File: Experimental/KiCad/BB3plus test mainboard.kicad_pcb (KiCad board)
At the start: 4 copper layers, 180.5 x 176 mm, 290 parts, among them IC1 SN74HCS02PWR, IC10 TPS62933ODRLR, IC11 FUSB303BTMX, IC12 TPS2068E, IC13 RT9742SNGV, IC14 TPD4E001DRLR, IC15 TPD4E001DRLR, IC16 TPD12S016PWR, IC17 MIC2026A-1YM-TR, IC18 TPD4E001DRLR, IC2 TPS3851H18EDRBR, IC3 M24C32-DFDW6TP, IC4 STM32G071R8T6, IC5 TPA6205A1DGN, IC6 SN74LVC1G14DBVR, IC7 LM64460CPPQRYFRQ1, IC8 TPS62933ODRLR, IC9 USB5816C-I/KD, Q1 2N7002, Q2 2N7002, Q3 MMBT5401, Q4 MMBT5401, Q5 2N7002, Q6 DMP3013SFV-7, Q7 DMP3013SFV-7, SW1 WBL2UOAGQR05CLR, SW2 LP4EE1RBATY, SW3 PEC16-2215F-S0024, X1 1-2199230-6, X10 10018783-10101TLF, X11 77313-802-20LF, X12 77313-802-20LF, X13 10018783-10101TLF, X14 5051102091, X15 TBP03R1-350-10BE, X3 571-0400, X4 GSP1.9101.1, X5 PJ-002BH-SMT-TR, X6 USB4056-03-A, X7 0862-1J1T-43-F, X8 SS-53000-002, X9 5051102091, Y1 32.768KHz, Y2 VXM7-9032-25M0000000

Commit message: Gerbers update
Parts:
- X10: value 10018783-10101TLF -> 1001878410201TLF
- moved JP11 0.80 mm to (313.8, 88.2)
- moved JP15 0.80 mm to (412.4, 26.2)
- moved JP3 0.77 mm to (388.3, 109.2)
- moved JP7 0.77 mm to (388.3, 106.7)

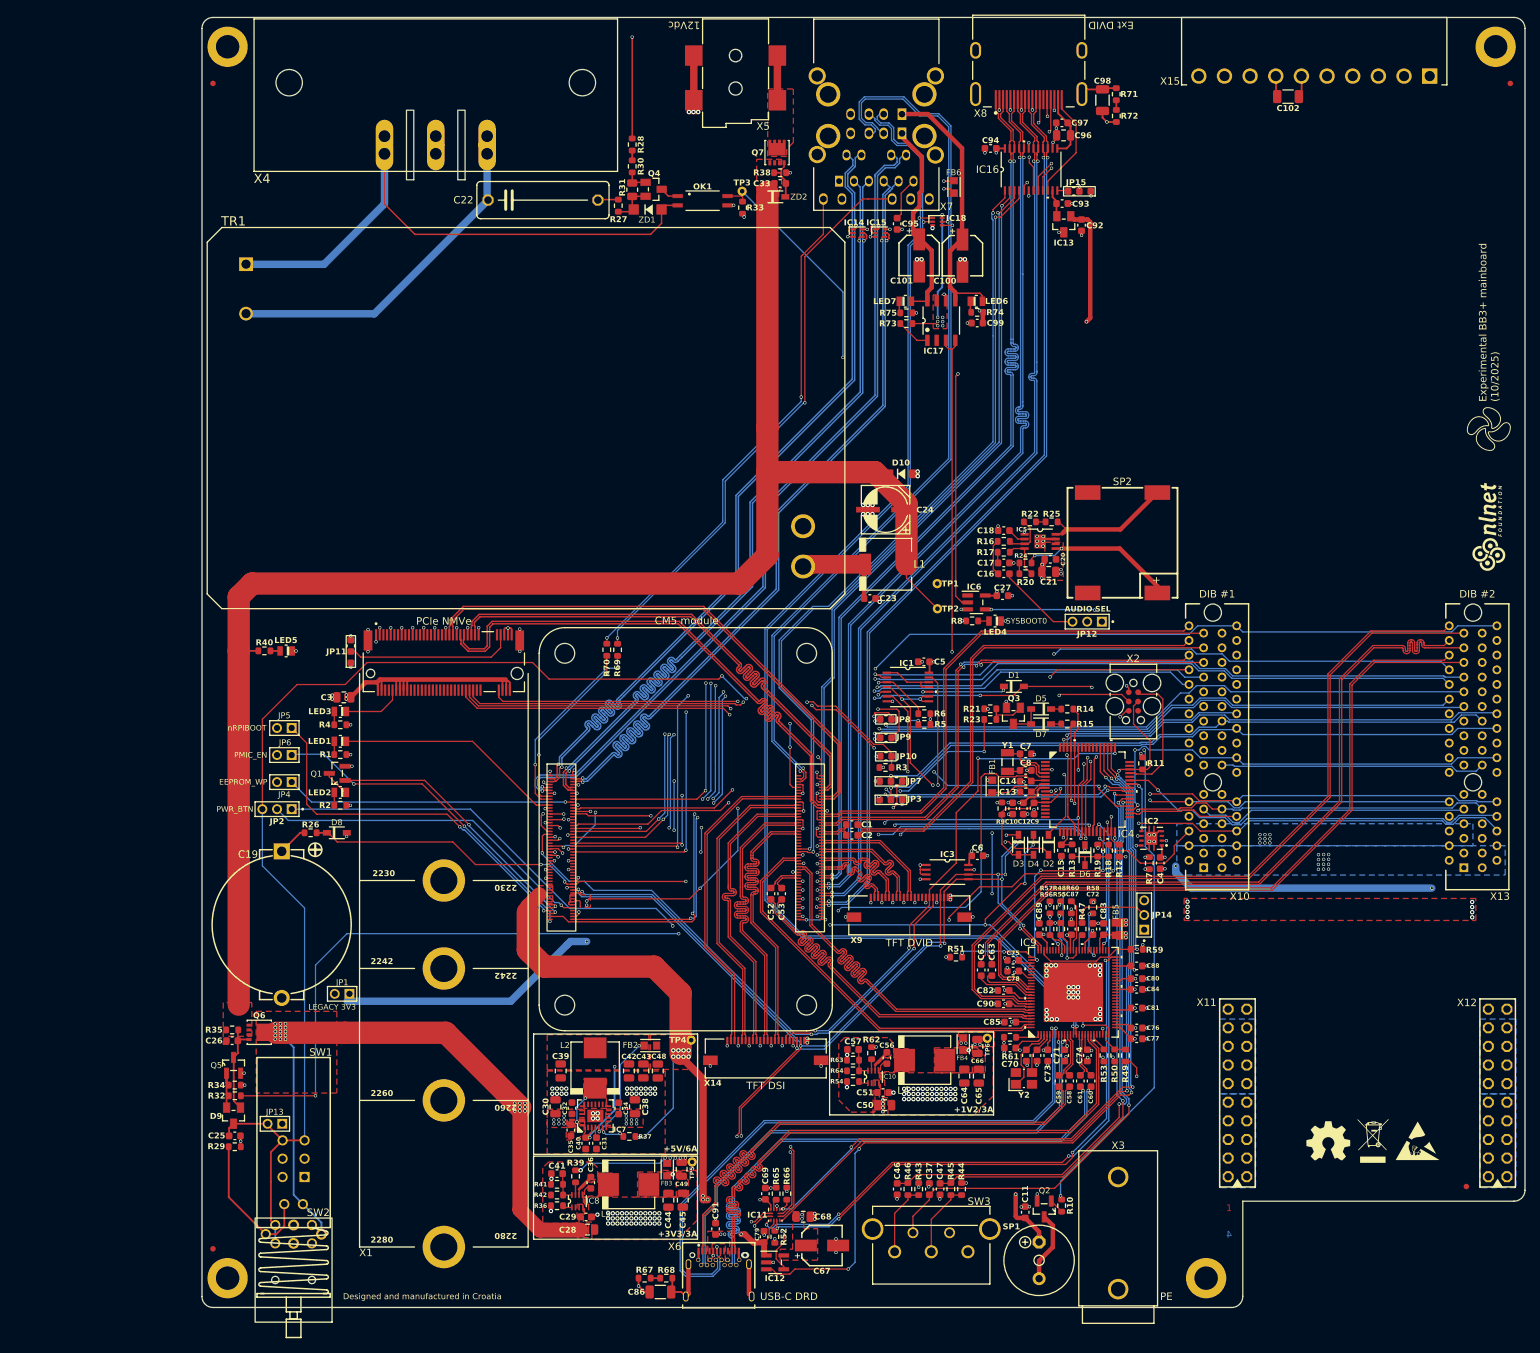
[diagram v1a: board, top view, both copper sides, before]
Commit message: Replace 3V3 jumper for H7 CM5 with PMOS sw
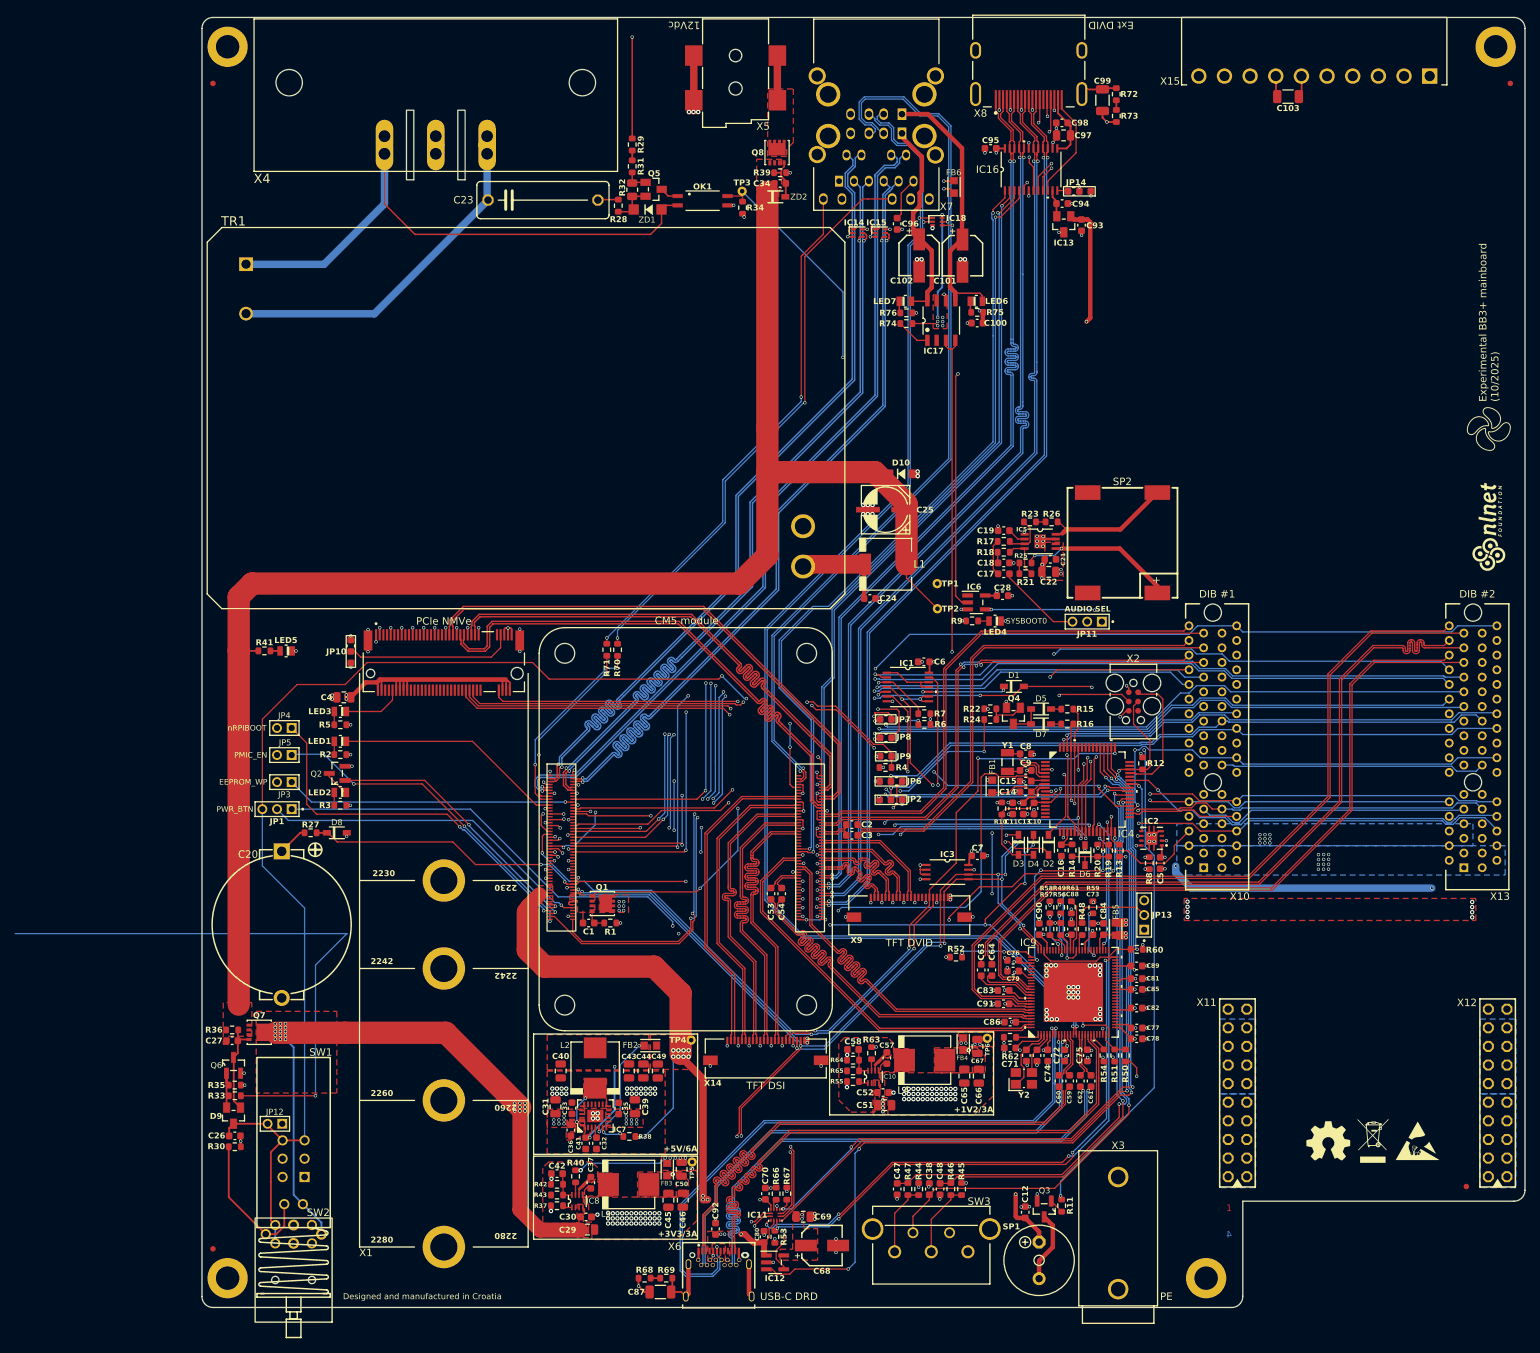
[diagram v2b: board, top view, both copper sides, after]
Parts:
- removed the JP1 at (312.6, 135.7)
- added C1: 100n, PCM_EEZ_passives:C_0603_1608Metric, F.Cu at (346.3, 126.0)
- added Q1: DMP3013SFV-7, PCM_EEZ_SMD:TRANS_FDMC8010, F.Cu at (348.1, 123.4)
- added R1: 10K, PCM_EEZ_passives:R_0603_1608Metric, F.Cu at (349.2, 126.0)
- renumbered C9 to C10, C99 to C100, C100 to C101, C101 to C102, C102 to C103, C10 to C11, C11 to C12, C12 to C13, C13 to C14, C14 to C15, C15 to C16, C16 to C17, C17 to C18, C18 to C19, C1 to C2, C19 to C20, C20 to C21, C21 to C22, C22 to C23, C23 to C24, C24 to C25, C25 to C26, C26 to C27, C27 to C28, C28 to C29, C2 to C3, C29 to C30, C30 to C31, C31 to C32, C32 to C33, C33 to C34, C34 to C35, C35 to C36, C36 to C37, C37 to C38, C38 to C39, C3 to C4, C39 to C40, C40 to C41, C41 to C42, C42 to C43, C43 to C44, C44 to C45, C45 to C46, C46 to C47, C47 to C48, C48 to C49, C4 to C5, C49 to C50, C50 to C51, C51 to C52, C52 to C53, C53 to C54, C54 to C55, C55 to C56, C56 to C57, C57 to C58, C58 to C59, C5 to C6, C59 to C60, C60 to C61, C61 to C62, C62 to C63, C63 to C64, C64 to C65, C65 to C66, C66 to C67, C67 to C68, C68 to C69, C6 to C7, C69 to C70, C70 to C71, C71 to C72, C72 to C73, C73 to C74, C74 to C75, C75 to C76, C76 to C77, C77 to C78, C78 to C79, C7 to C8, C79 to C80, C80 to C81, C81 to C82, C82 to C83, C83 to C84, C84 to C85, C85 to C86, C86 to C87, C87 to C88, C88 to C89, C8 to C9, C89 to C90, C90 to C91, C91 to C92, C92 to C93, C93 to C94, C94 to C95, C95 to C96, C96 to C97, C97 to C98, C98 to C99, JP2 to JP1, JP11 to JP10, JP12 to JP11, JP13 to JP12, JP14 to JP13, JP15 to JP14, JP3 to JP2, JP4 to JP3, JP5 to JP4, JP6 to JP5, JP7 to JP6, JP8 to JP7, JP9 to JP8, JP10 to JP9, Q1 to Q2, Q2 to Q3, Q3 to Q4, Q4 to Q5, Q5 to Q6, Q6 to Q7, Q7 to Q8, R9 to R10, R10 to R11, R11 to R12, R12 to R13, R13 to R14, R14 to R15, R15 to R16, R16 to R17, R17 to R18, R18 to R19, R1 to R2, R19 to R20, R20 to R21, R21 to R22, R22 to R23, R23 to R24, R24 to R25, R25 to R26, R26 to R27, R27 to R28, R28 to R29, R2 to R3, R29 to R30, R30 to R31, R31 to R32, R32 to R33, R33 to R34, R34 to R35, R35 to R36, R36 to R37, R37 to R38, R38 to R39, R3 to R4, R39 to R40, R40 to R41, R41 to R42, R42 to R43, R43 to R44, R44 to R45, R45 to R46, R46 to R47, R47 to R48, R48 to R49, R4 to R5, R49 to R50, R50 to R51, R51 to R52, R52 to R53, R53 to R54, R54 to R55, R55 to R56, R56 to R57, R57 to R58, R58 to R59, R5 to R6, R59 to R60, R60 to R61, R61 to R62, R62 to R63, R63 to R64, R64 to R65, R65 to R66, R66 to R67, R67 to R68, R68 to R69, R6 to R7, R69 to R70, R70 to R71, R71 to R72, R72 to R73, R73 to R74, R74 to R75, R75 to R76, R7 to R8, R8 to R9
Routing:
- net I2C_PU_BIAS: track 111.8 -> 71.0 mm, vias 7 -> 4
- net Net-(Module1A-CAM_GPIO1): track 59.9 -> 64.2 mm
- net Net-(Q1-G): track 0.00 -> 3.31 mm
- net Net-(Module1A-CAM_GPIO0): track 66.5 -> 69.7 mm
- net GND: track 87.7 -> 87.1 mm, vias 337 -> 338
- net +3V3: vias 57 -> 63
